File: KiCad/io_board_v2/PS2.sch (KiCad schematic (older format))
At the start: 9 parts, among them J2 Keyboard, U3 74HC07, U4 74HCT04, U5 8042

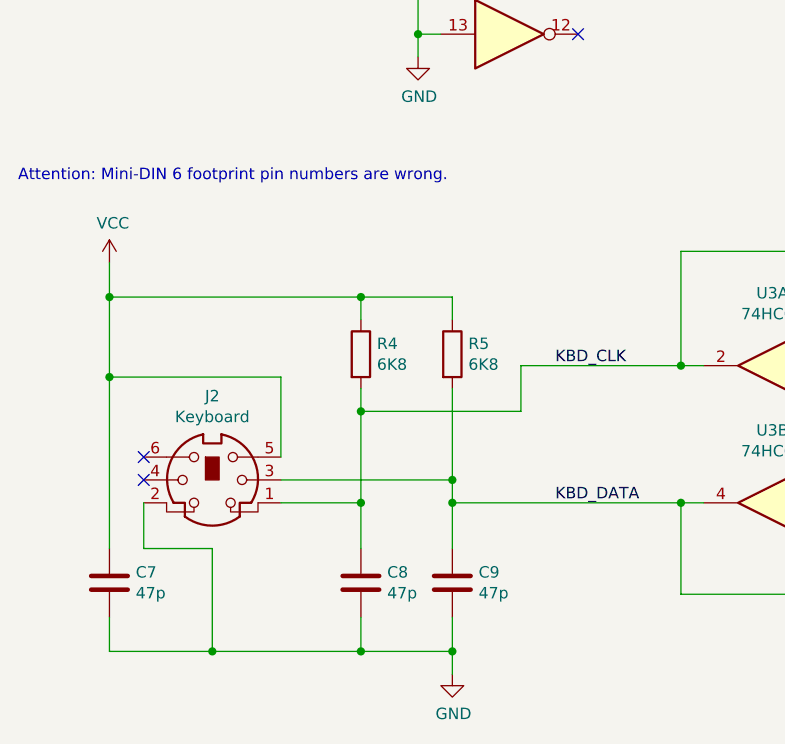
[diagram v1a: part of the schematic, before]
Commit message: Fixed wrong Mini-DIN 6 footprint.
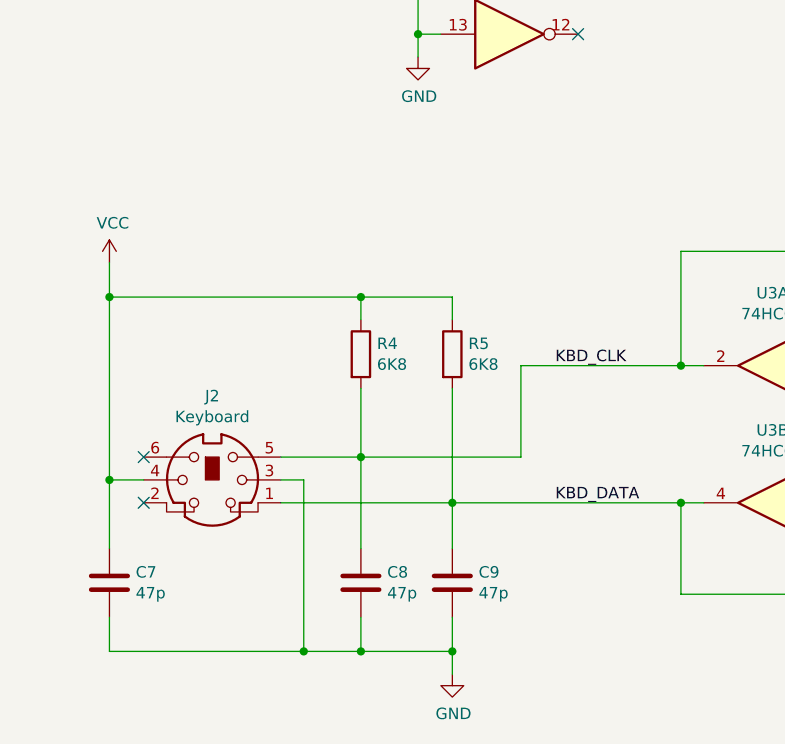
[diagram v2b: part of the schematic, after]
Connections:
- net GND: now also J2.3; no longer J2.2
- net KBD_CLK: now also J2.5; no longer J2.1
- net KBD_DATA: now also J2.1; no longer J2.3
- net VCC: now also J2.4; no longer J2.5
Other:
- note removed: "Attention: Mini-DIN 6 footprint pin numbers are wrong.\n"
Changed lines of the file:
@@
 Title "Mini8086 I/O board"
 Date "2020-11-05"
-Rev "2.0"
+Rev "1.2"
 Comp ""
 Comment1 ""
@@
 Connection ~ 4300 4700
 Wire Wire Line
-	3600 4300 3600 4100
+	3600 4500 3600 4100
 Wire Wire Line
 	3600 4100 4300 4100
-Wire Wire Line
-	2900 4900 2900 4700
-Connection ~ 2900 4300
-Wire Wire Line
-	2900 4300 3600 4300
+Connection ~ 2900 4500
+Wire Wire Line
+	2900 4500 3600 4500
 Wire Wire Line
 	3300 4900 3300 4700
@@
 $EndComp
 Wire Wire Line
-	3300 4200 3300 4600
-Wire Wire Line
-	2900 4200 2900 4300
+	2900 4200 2900 4500
 Wire Wire Line
 	2900 3900 2900 3800
@@
 Text Label 8300 4800 0    50   ~ 0
 ~PCLK
-Wire Wire Line
-	1800 5350 2250 5350
-Wire Wire Line
-	1800 3800 1800 4150
-Wire Wire Line
-	2550 4700 2900 4700
-Connection ~ 2900 4700
-Wire Wire Line
-	2900 4700 2900 4300
-Wire Wire Line
-	1950 4700 1950 4900
-Wire Wire Line
-	1950 4900 2250 4900
-Wire Wire Line
-	2250 4900 2250 5350
-Connection ~ 2250 5350
-Wire Wire Line
-	2250 5350 2900 5350
-Wire Wire Line
-	2550 4600 3300 4600
-Connection ~ 3300 4600
-Wire Wire Line
-	3300 4600 3300 4700
-Wire Wire Line
-	2550 4500 2550 4150
-Wire Wire Line
-	2550 4150 1800 4150
-Connection ~ 1800 4150
-Wire Wire Line
-	1800 4150 1800 4900
-NoConn ~ 1950 4600
-NoConn ~ 1950 4500
-Text Notes 1400 3300 0    50   ~ 0
-Attention: Mini-DIN 6 footprint pin numbers are wrong.\n
 $Comp
 L 74xx:74HC04 U3
@@
 NoConn ~ 3850 1650
 NoConn ~ 3850 1150
+Wire Wire Line
+	3300 4200 3300 4700
+Wire Wire Line
+	1800 3800 1800 4600
+Wire Wire Line
+	1800 5350 2650 5350
+NoConn ~ 1950 4700
+NoConn ~ 1950 4500
+Wire Wire Line
+	1950 4600 1800 4600
+Connection ~ 1800 4600
+Wire Wire Line
+	1800 4600 1800 4900
+Wire Wire Line
+	2550 4500 2900 4500
+Wire Wire Line
+	2900 4500 2900 4900
+Wire Wire Line
+	2550 4700 3300 4700
+Wire Wire Line
+	2550 4600 2650 4600
+Wire Wire Line
+	2650 4600 2650 5350
+Connection ~ 2650 5350
+Wire Wire Line
+	2650 5350 2900 5350
 Wire Bus Line
 	8650 2650 8650 3400

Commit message: Fixed wrong symbol, added comment.
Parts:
- removed unit 3 of U3
- removed unit 4 of U3
- removed unit 5 of U3
- removed unit 6 of U3
- added unit 3 of U3
- added unit 4 of U3
- added unit 5 of U3
- added unit 6 of U3
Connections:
- net GND: now also U3.11, U3.13, U3.5, U3.9
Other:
- note added: "U3 maybe 74HC06 for some keyboard controllers."
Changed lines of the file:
@@
 ~PCLK
-$Comp
-L 74xx:74HC04 U3
-U 3 1 60241E6C
-P 3550 1150
-F 0 "U3" H 3550 1467 50  0000 C CNN
-F 1 "74HC07" H 3550 1376 50  0000 C CNN
-F 2 "Package_SO:SOIC-14_3.9x8.7mm_P1.27mm" H 3550 1150 50  0001 C CNN
-F 3 "https://assets.nexperia.com/documents/data-sheet/74HC_HCT04.pdf" H 3550 1150 50  0001 C CNN
-	3    3550 1150
-	1    0    0    -1
-$EndComp
-$Comp
-L 74xx:74HC04 U3
-U 4 1 60242776
-P 3550 1650
-F 0 "U3" H 3550 1967 50  0000 C CNN
-F 1 "74HC07" H 3550 1876 50  0000 C CNN
-F 2 "Package_SO:SOIC-14_3.9x8.7mm_P1.27mm" H 3550 1650 50  0001 C CNN
-F 3 "https://assets.nexperia.com/documents/data-sheet/74HC_HCT04.pdf" H 3550 1650 50  0001 C CNN
-	4    3550 1650
-	1    0    0    -1
-$EndComp
-$Comp
-L 74xx:74HC04 U3
-U 5 1 60243D7A
-P 3550 2150
-F 0 "U3" H 3550 2467 50  0000 C CNN
-F 1 "74HC07" H 3550 2376 50  0000 C CNN
-F 2 "Package_SO:SOIC-14_3.9x8.7mm_P1.27mm" H 3550 2150 50  0001 C CNN
-F 3 "https://assets.nexperia.com/documents/data-sheet/74HC_HCT04.pdf" H 3550 2150 50  0001 C CNN
-	5    3550 2150
-	1    0    0    -1
-$EndComp
-$Comp
-L 74xx:74HC04 U3
-U 6 1 602448F9
-P 3550 2650
-F 0 "U3" H 3550 2967 50  0000 C CNN
-F 1 "74HC07" H 3550 2876 50  0000 C CNN
-F 2 "Package_SO:SOIC-14_3.9x8.7mm_P1.27mm" H 3550 2650 50  0001 C CNN
-F 3 "https://assets.nexperia.com/documents/data-sheet/74HC_HCT04.pdf" H 3550 2650 50  0001 C CNN
-	6    3550 2650
-	1    0    0    -1
-$EndComp
 $Comp
 L power:GND #PWR0116
@@
 Wire Bus Line
 	8650 2650 8650 3400
+$Comp
+L 74xx:SN74LS07N U3
+U 3 1 616DF698
+P 3550 2650
+F 0 "U3" H 3550 2333 50  0000 C CNN
+F 1 "74HC07" H 3550 2424 50  0000 C CNN
+F 2 "Package_SO:SOIC-14_3.9x8.7mm_P1.27mm" H 3550 2650 50  0001 C CNN
+F 3 "https://assets.nexperia.com/documents/data-sheet/74HC_HCT04.pdf" H 3550 2650 50  0001 C CNN
+	3    3550 2650
+	1    0    0    -1
+$EndComp
+$Comp
+L 74xx:SN74LS07N U3
+U 4 1 616E0C03
+P 3550 2150
+F 0 "U3" H 3550 1833 50  0000 C CNN
+F 1 "74HC07" H 3550 1924 50  0000 C CNN
+F 2 "Package_SO:SOIC-14_3.9x8.7mm_P1.27mm" H 3550 2150 50  0001 C CNN
+F 3 "https://assets.nexperia.com/documents/data-sheet/74HC_HCT04.pdf" H 3550 2150 50  0001 C CNN
+	4    3550 2150
+	1    0    0    -1
+$EndComp
+$Comp
+L 74xx:SN74LS07N U3
+U 5 1 616E1299
+P 3550 1650
+F 0 "U3" H 3550 1333 50  0000 C CNN
+F 1 "74HC07" H 3550 1424 50  0000 C CNN
+F 2 "Package_SO:SOIC-14_3.9x8.7mm_P1.27mm" H 3550 1650 50  0001 C CNN
+F 3 "https://assets.nexperia.com/documents/data-sheet/74HC_HCT04.pdf" H 3550 1650 50  0001 C CNN
+	5    3550 1650
+	1    0    0    -1
+$EndComp
+$Comp
+L 74xx:SN74LS07N U3
+U 6 1 616E178A
+P 3550 1150
+F 0 "U3" H 3550 833 50  0000 C CNN
+F 1 "74HC07" H 3550 924 50  0000 C CNN
+F 2 "Package_SO:SOIC-14_3.9x8.7mm_P1.27mm" H 3550 1150 50  0001 C CNN
+F 3 "https://assets.nexperia.com/documents/data-sheet/74HC_HCT04.pdf" H 3550 1150 50  0001 C CNN
+	6    3550 1150
+	1    0    0    -1
+$EndComp
+Text Notes 4150 3450 0    50   ~ 0
+U3 maybe 74HC06 for some keyboard controllers.
 $EndSCHEMATC

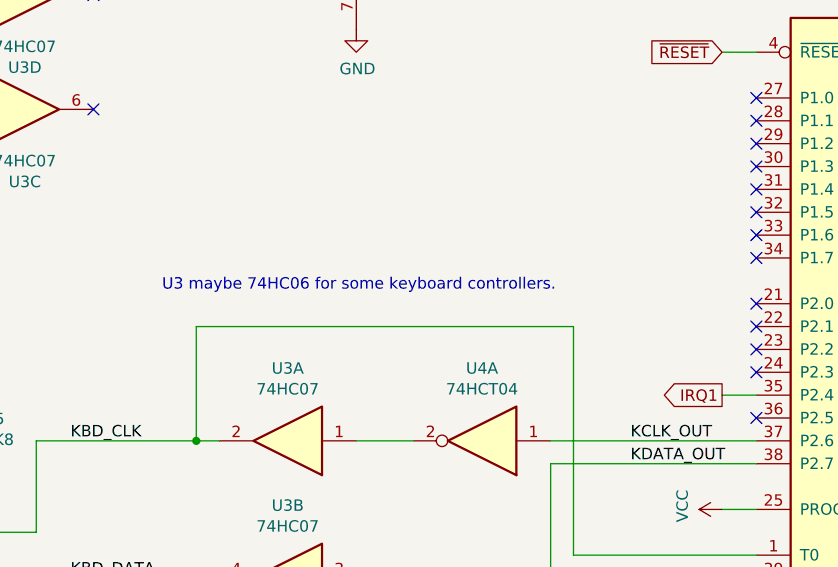
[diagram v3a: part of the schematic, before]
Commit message: Adds fix for VT82C42 keyboard controller.
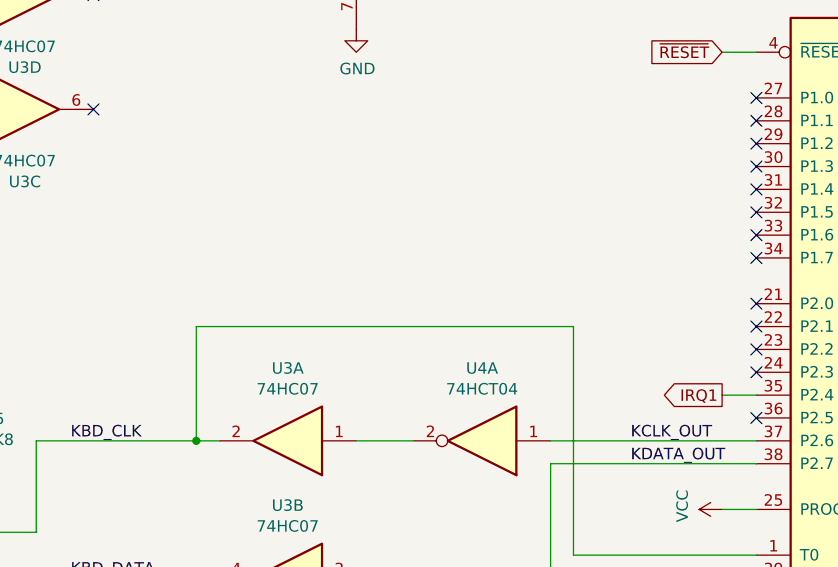
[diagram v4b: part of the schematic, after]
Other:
- note removed: "U3 maybe 74HC06 for some keyboard controllers."
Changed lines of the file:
@@
 Wire Wire Line
 	2650 5350 2900 5350
-Wire Bus Line
-	8650 2650 8650 3400
 $Comp
 L 74xx:SN74LS07N U3
@@
 	1    0    0    -1
 $EndComp
-Text Notes 4150 3450 0    50   ~ 0
-U3 maybe 74HC06 for some keyboard controllers.
+Wire Bus Line
+	8650 2650 8650 3400
 $EndSCHEMATC
